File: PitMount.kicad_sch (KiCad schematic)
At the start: 15 parts, among them J1 Conn_01x07, Q1 BC817, Q2 IRLML6401, U1 UnifyNano, U2 ELRS-Rx

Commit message: Fix resistor LCSC reference
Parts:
- R3: LCSC C3015779 -> C3015779
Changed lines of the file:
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@@
       (effects (font (size 1.27 1.27)) hide)
     )
-    (property "LCSC" "C3015779 " (id 4) (at 90.17 85.09 0)
+    (property "LCSC" "C3015779" (id 4) (at 90.17 85.09 0)
       (effects (font (size 1.27 1.27)) hide)
     )

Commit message: Use new mounting hole footprint
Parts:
- H1, H2, H3, H4: footprint MountingHole:MountingHole_3.2mm_M3_DIN965_Pad -> PitMount:3.2mm_PTH
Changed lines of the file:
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@@
       (effects (font (size 1.27 1.27)) (justify left))
     )
-    (property "Footprint" "MountingHole:MountingHole_3.2mm_M3_DIN965_Pad" (id 2) (at 195.58 30.48 0)
+    (property "Footprint" "PitMount:3.2mm_PTH" (id 2) (at 195.58 30.48 0)
       (effects (font (size 1.27 1.27)) hide)
     )
@@
       (effects (font (size 1.27 1.27)) (justify left))
     )
-    (property "Footprint" "MountingHole:MountingHole_3.2mm_M3_DIN965_Pad" (id 2) (at 195.58 26.035 0)
+    (property "Footprint" "PitMount:3.2mm_PTH" (id 2) (at 195.58 26.035 0)
       (effects (font (size 1.27 1.27)) hide)
     )
@@
       (effects (font (size 1.27 1.27)) (justify left))
     )
-    (property "Footprint" "MountingHole:MountingHole_3.2mm_M3_DIN965_Pad" (id 2) (at 195.58 34.925 0)
+    (property "Footprint" "PitMount:3.2mm_PTH" (id 2) (at 195.58 34.925 0)
       (effects (font (size 1.27 1.27)) hide)
     )
@@
       (effects (font (size 1.27 1.27)) (justify left))
     )
-    (property "Footprint" "MountingHole:MountingHole_3.2mm_M3_DIN965_Pad" (id 2) (at 195.58 39.37 0)
+    (property "Footprint" "PitMount:3.2mm_PTH" (id 2) (at 195.58 39.37 0)
       (effects (font (size 1.27 1.27)) hide)
     )
@@
     )
     (path "/5890d34d-218f-435b-ba67-2017655ebfa5"
-      (reference "H1") (unit 1) (value "MountingHole_Pad") (footprint "MountingHole:MountingHole_3.2mm_M3_DIN965_Pad")
+      (reference "H1") (unit 1) (value "MountingHole_Pad") (footprint "PitMount:3.2mm_PTH")
     )
     (path "/24804176-3315-4716-8bbc-e01bf025e551"
-      (reference "H2") (unit 1) (value "MountingHole_Pad") (footprint "MountingHole:MountingHole_3.2mm_M3_DIN965_Pad")
+      (reference "H2") (unit 1) (value "MountingHole_Pad") (footprint "PitMount:3.2mm_PTH")
     )
     (path "/dd4773b8-24bf-4708-8f9f-f8fb2d44b2c4"
-      (reference "H3") (unit 1) (value "MountingHole_Pad") (footprint "MountingHole:MountingHole_3.2mm_M3_DIN965_Pad")
+      (reference "H3") (unit 1) (value "MountingHole_Pad") (footprint "PitMount:3.2mm_PTH")
     )
     (path "/e7a0c2e5-a9b9-458f-a634-e124b119ebea"
-      (reference "H4") (unit 1) (value "MountingHole_Pad") (footprint "MountingHole:MountingHole_3.2mm_M3_DIN965_Pad")
+      (reference "H4") (unit 1) (value "MountingHole_Pad") (footprint "PitMount:3.2mm_PTH")
     )
     (path "/30f01af8-011a-470c-8d41-9a0d8369203a"

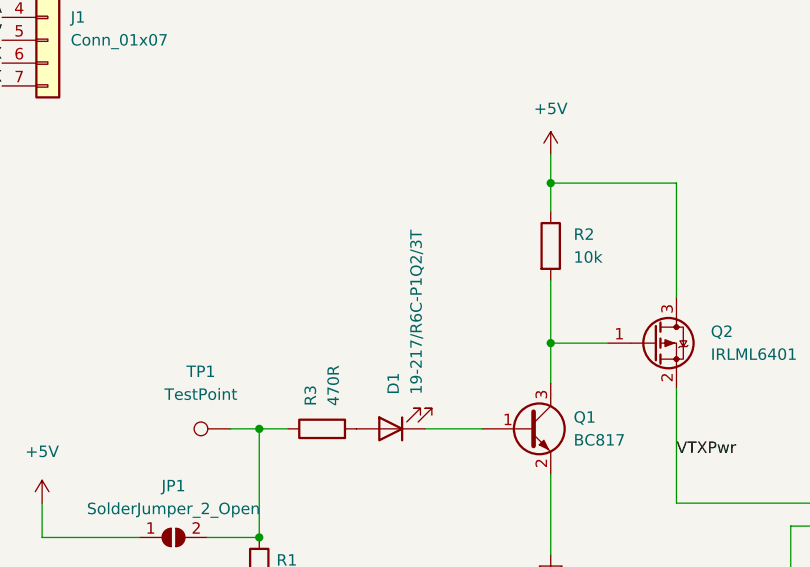
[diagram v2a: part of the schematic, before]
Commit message: Make LED a 0402 component
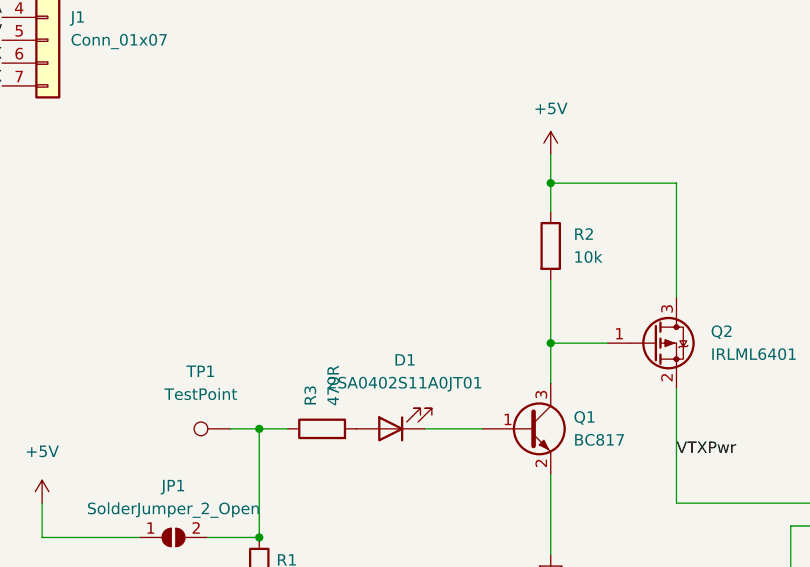
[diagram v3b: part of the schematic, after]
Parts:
- D1: value 19-217/R6C-P1Q2/3T -> 2SA0402S11A0JT01; footprint LED_SMD:LED_0603_1608Metric -> LED_SMD:LED_0402_1005Metric; LCSC C142276 -> C233194
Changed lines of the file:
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@@
   (symbol (lib_id "Device:LED") (at 97.79 85.09 180) (unit 1)
     (in_bom yes) (on_board yes) (fields_autoplaced)
-    (property "Reference" "D1" (id 0) (at 98.1074 81.28 90)
-      (effects (font (size 1.27 1.27)) (justify right))
-    )
-    (property "Value" "19-217/R6C-P1Q2/3T" (id 1) (at 100.6474 81.28 90)
-      (effects (font (size 1.27 1.27)) (justify right))
-    )
-    (property "Footprint" "LED_SMD:LED_0603_1608Metric" (id 2) (at 97.79 85.09 0)
-      (effects (font (size 1.27 1.27)) hide)
-    )
-    (property "Datasheet" "https://datasheet.lcsc.com/lcsc/1809111512_Everlight-Elec-19-217-R6C-P1Q2-3T_C142276.pdf" (id 3) (at 97.79 85.09 0)
-      (effects (font (size 1.27 1.27)) hide)
-    )
-    (property "LCSC" "C142276" (id 4) (at 97.79 85.09 0)
+    (property "Reference" "D1" (id 0) (at 99.3775 77.47 0))
+    (property "Value" "2SA0402S11A0JT01" (id 1) (at 99.3775 80.01 0))
+    (property "Footprint" "LED_SMD:LED_0402_1005Metric" (id 2) (at 97.79 85.09 0)
+      (effects (font (size 1.27 1.27)) hide)
+    )
+    (property "Datasheet" "https://datasheet.lcsc.com/lcsc/1808291043_Brightek-Optoelectronics-2SA0402S11A0JT01_C233194.pdf" (id 3) (at 97.79 85.09 0)
+      (effects (font (size 1.27 1.27)) hide)
+    )
+    (property "LCSC" "C233194" (id 4) (at 97.79 85.09 0)
       (effects (font (size 1.27 1.27)) hide)
     )
@@
     )
     (path "/1b8c00fa-e7ad-4458-b438-f3f4ef6a5d07"
-      (reference "D1") (unit 1) (value "19-217/R6C-P1Q2/3T") (footprint "LED_SMD:LED_0603_1608Metric")
+      (reference "D1") (unit 1) (value "2SA0402S11A0JT01") (footprint "LED_SMD:LED_0402_1005Metric")
     )
     (path "/5890d34d-218f-435b-ba67-2017655ebfa5"

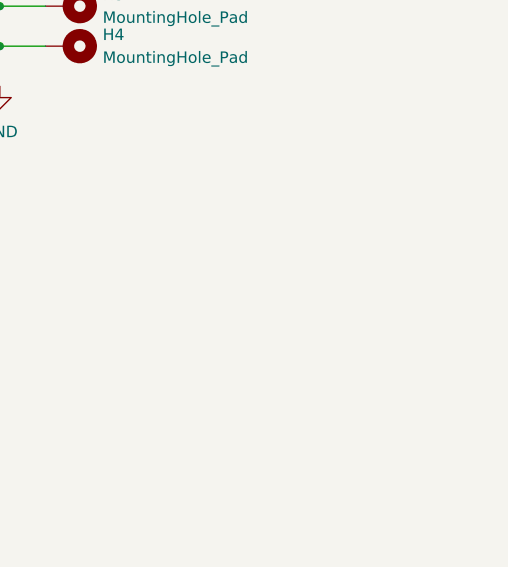
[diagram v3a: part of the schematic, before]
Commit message: Add tooling holes to schematics
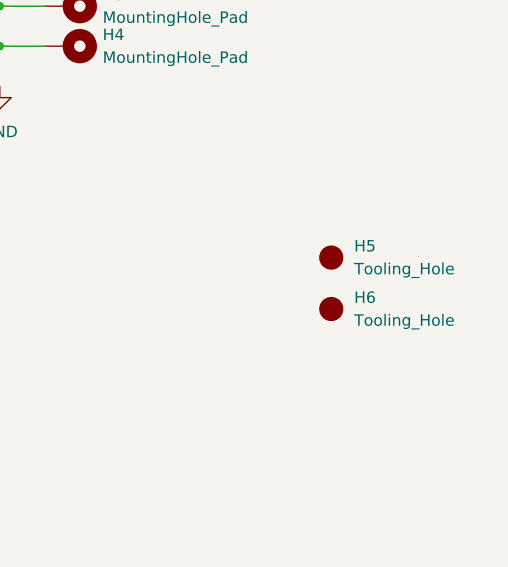
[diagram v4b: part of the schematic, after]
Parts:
- added H5, H6: Tooling_Hole, PitMount:Tooling Hole, symbol PitMount:Tooling_Hole
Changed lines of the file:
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@@
     (effects (font (size 1.27 1.27)) (justify right bottom))
+  )
+  (symbol (lib_id "PitMount:Tooling_Hole") (at 224.79 62.865 0) (unit 1)
+    (in_bom yes) (on_board yes) (fields_autoplaced)
+    (property "Reference" "H5" (id 0) (at 227.33 61.5949 0)
+      (effects (font (size 1.27 1.27)) (justify left))
+    )
+    (property "Value" "Tooling_Hole" (id 1) (at 227.33 64.1349 0)
+      (effects (font (size 1.27 1.27)) (justify left))
+    )
+    (property "Footprint" "PitMount:Tooling Hole" (id 2) (at 224.79 60.325 0)
+      (effects (font (size 1.27 1.27)) hide)
+    )
+    (property "Datasheet" "" (id 3) (at 224.79 60.325 0)
+      (effects (font (size 1.27 1.27)) hide)
+    )
   )
   (symbol (lib_id "Device:R") (at 90.17 85.09 90) (unit 1)
@@
     (pin "3")
   )
+  (symbol (lib_id "PitMount:Tooling_Hole") (at 224.79 68.58 0) (unit 1)
+    (in_bom yes) (on_board yes) (fields_autoplaced)
+    (property "Reference" "H6" (id 0) (at 227.33 67.3099 0)
+      (effects (font (size 1.27 1.27)) (justify left))
+    )
+    (property "Value" "Tooling_Hole" (id 1) (at 227.33 69.8499 0)
+      (effects (font (size 1.27 1.27)) (justify left))
+    )
+    (property "Footprint" "PitMount:Tooling Hole" (id 2) (at 224.79 66.04 0)
+      (effects (font (size 1.27 1.27)) hide)
+    )
+    (property "Datasheet" "" (id 3) (at 224.79 66.04 0)
+      (effects (font (size 1.27 1.27)) hide)
+    )
+  )
   (sheet_instances
     (path "/" (page "1"))
@@
       (reference "H4") (unit 1) (value "MountingHole_Pad") (footprint "PitMount:3.2mm_PTH")
     )
+    (path "/00c4b040-0c0a-44f7-a83c-745c7e9f586a"
+      (reference "H5") (unit 1) (value "Tooling_Hole") (footprint "PitMount:Tooling Hole")
+    )
+    (path "/f428637f-a06f-4f51-8742-a62625c7eb79"
+      (reference "H6") (unit 1) (value "Tooling_Hole") (footprint "PitMount:Tooling Hole")
+    )
     (path "/30f01af8-011a-470c-8d41-9a0d8369203a"

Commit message: Change resistor type
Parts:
- R3: LCSC C3015779 -> C114877
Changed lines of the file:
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@@
       (effects (font (size 1.27 1.27)) hide)
     )
-    (property "LCSC" "C3015779" (id 4) (at 90.17 85.09 0)
+    (property "LCSC" "C114877" (id 4) (at 90.17 85.09 0)
       (effects (font (size 1.27 1.27)) hide)
     )

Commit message: Change LED type
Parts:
- D1: LCSC C233194 -> C71911
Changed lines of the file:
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@@
       (effects (font (size 1.27 1.27)) hide)
     )
-    (property "Datasheet" "https://datasheet.lcsc.com/lcsc/1808291043_Brightek-Optoelectronics-2SA0402S11A0JT01_C233194.pdf" (id 3) (at 97.79 85.09 0)
+    (property "Datasheet" "https://datasheet.lcsc.com/lcsc/1806151119_Everlight-Elec-16-213-SDRC-S530-A3-TR8_C71911.pdf" (id 3) (at 97.79 85.09 0)
       (effects (font (size 1.27 1.27)) hide)
     )
-    (property "LCSC" "C233194" (id 4) (at 97.79 85.09 0)
+    (property "LCSC" "C71911" (id 4) (at 97.79 85.09 0)
       (effects (font (size 1.27 1.27)) hide)
     )

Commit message: Update project files with version 7.0-rc1
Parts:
- Q1, Q2: JLCPCB Rotation Offset (none) -> 180

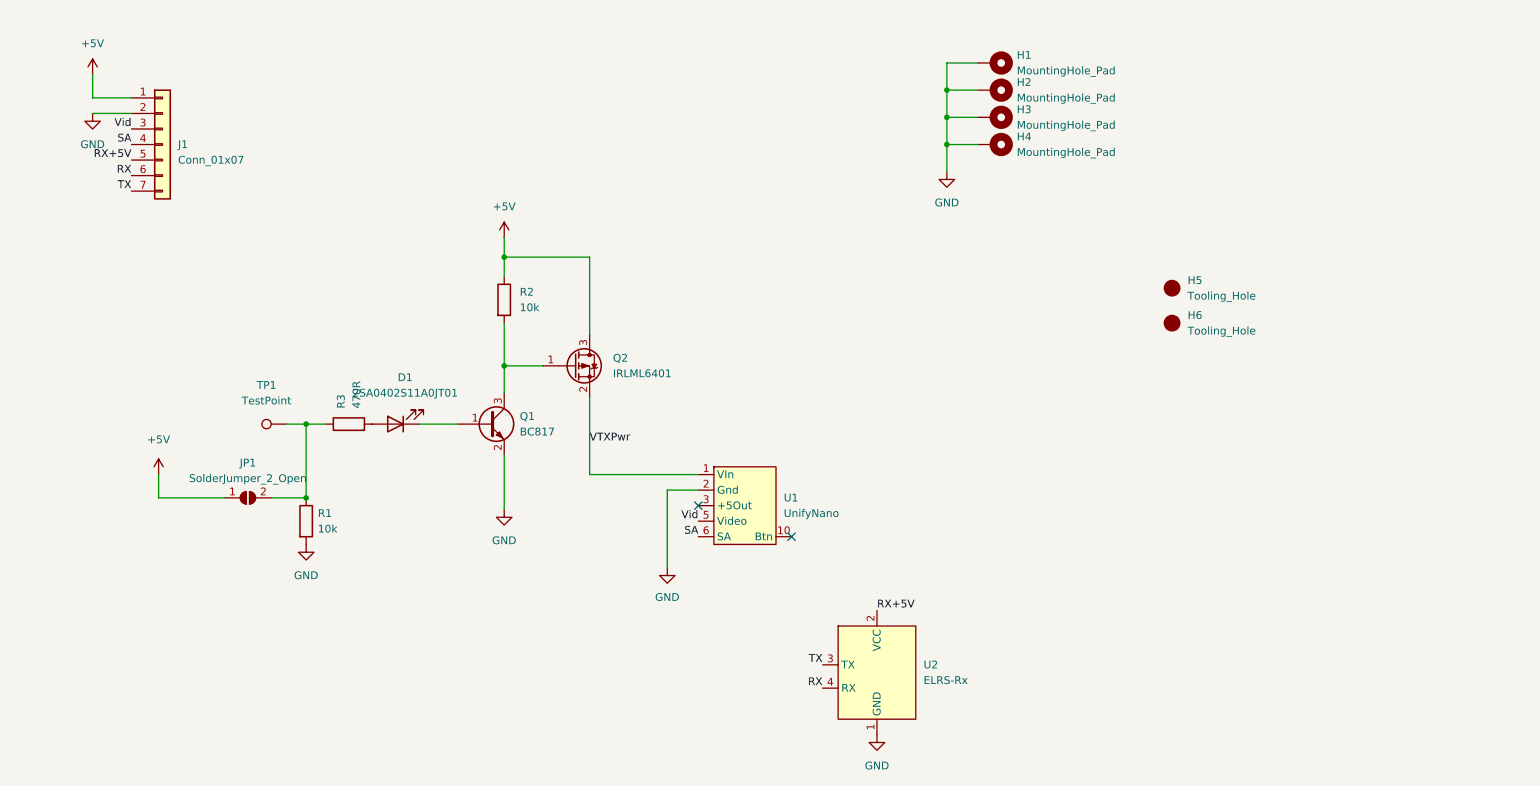
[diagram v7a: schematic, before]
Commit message: Update schematic file
- Change solder connector to 8-pin
- Change footprint of LED to 0603
- Use basic parts where possible
- Compact FET drawing
- Remove tooling holes
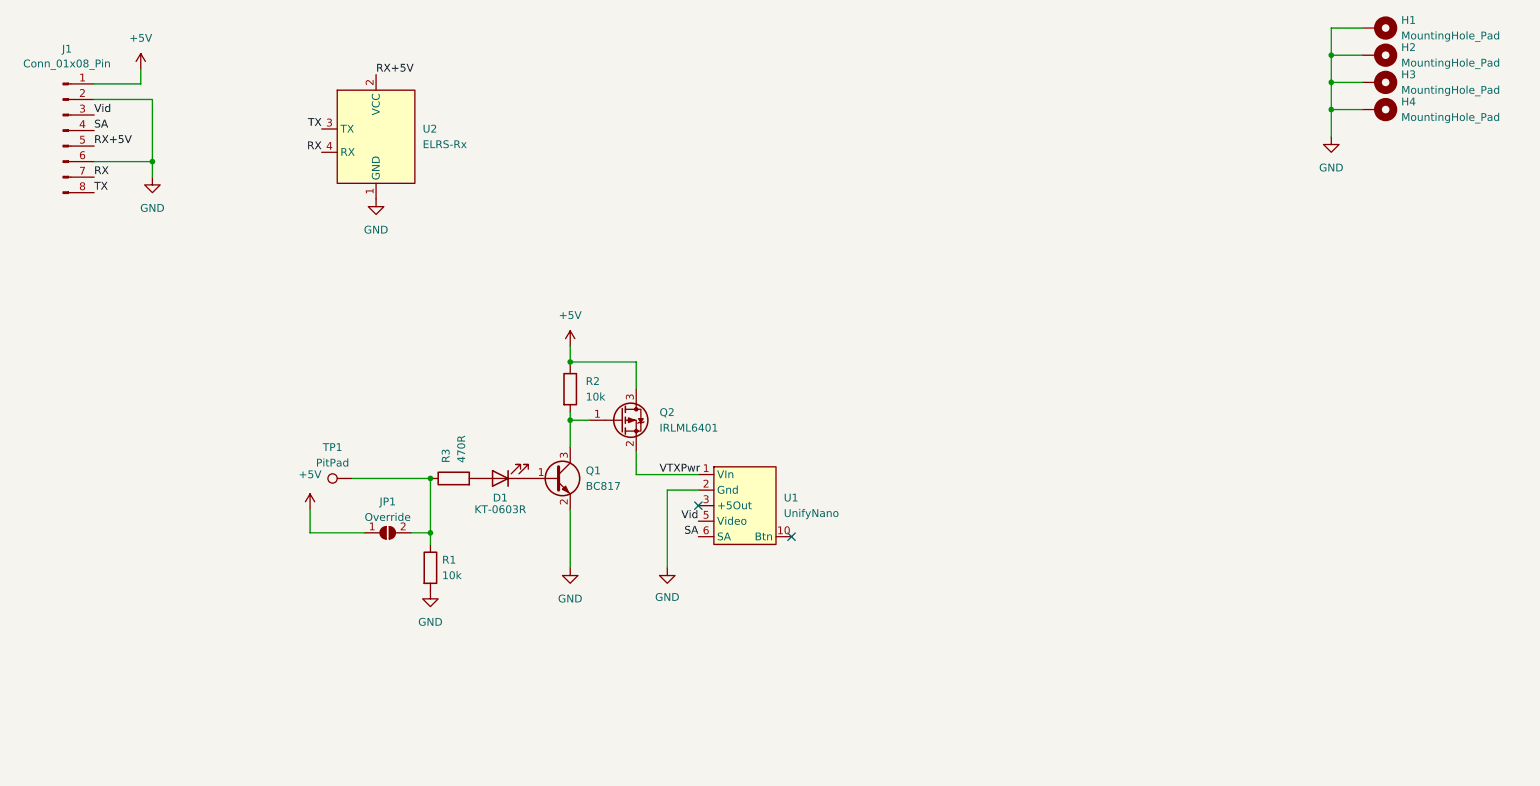
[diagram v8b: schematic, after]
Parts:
- removed H5, H6: Tooling_Hole, PitMount:Tooling Hole, symbol PitMount:Tooling_Hole
- removed J1: Conn_01x07, PitMount:VTXConn, symbol Connector_Generic:Conn_01x07
- added J1: Conn_01x08_Pin, PitMount:VTXConn, symbol Connector:Conn_01x08_Pin
- D1: value 2SA0402S11A0JT01 -> KT-0603R; footprint LED_SMD:LED_0402_1005Metric -> LED_SMD:LED_0603_1608Metric; LCSC C71911 -> C2286
- JP1: value SolderJumper_2_Open -> Override
- R1, R2: LCSC C3015825 -> C25744
- R3: LCSC C114877 -> C25117
- TP1: value TestPoint -> PitPad
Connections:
- net +5V: now also J1.1 (Pin_1)
- net GND: now also J1.2 (Pin_2), J1.6 (Pin_6)
- net RX: now also J1.7 (Pin_7)
- net RX+5V: now also J1.5 (Pin_5)
- net SA: now also J1.4 (Pin_4)
- net TX: now also J1.8 (Pin_8)
- net Vid: now also J1.3 (Pin_3)
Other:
- moved on the sheet: D1, H1, H2, H3, H4, JP1, Q1, Q2, R1, R2, R3, TP1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
